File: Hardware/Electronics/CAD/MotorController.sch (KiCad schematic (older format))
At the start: 11 parts, among them J1 MPE 094-1-006, J2 CONN_01X03, J5 CONN_01X04, SW2 SW_DPST_x2, U1 LD1117S33CTR, U2 Nema17, U3 TMC2130, U4 ESP-12E

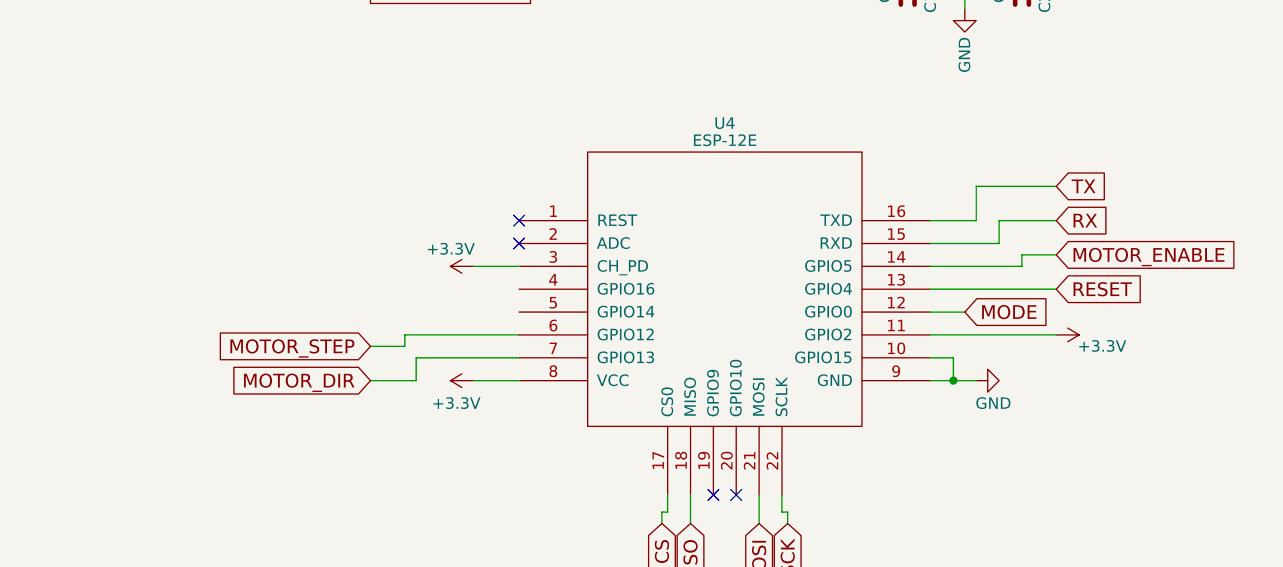
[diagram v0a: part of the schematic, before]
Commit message: home automation iplementation of motor controller software
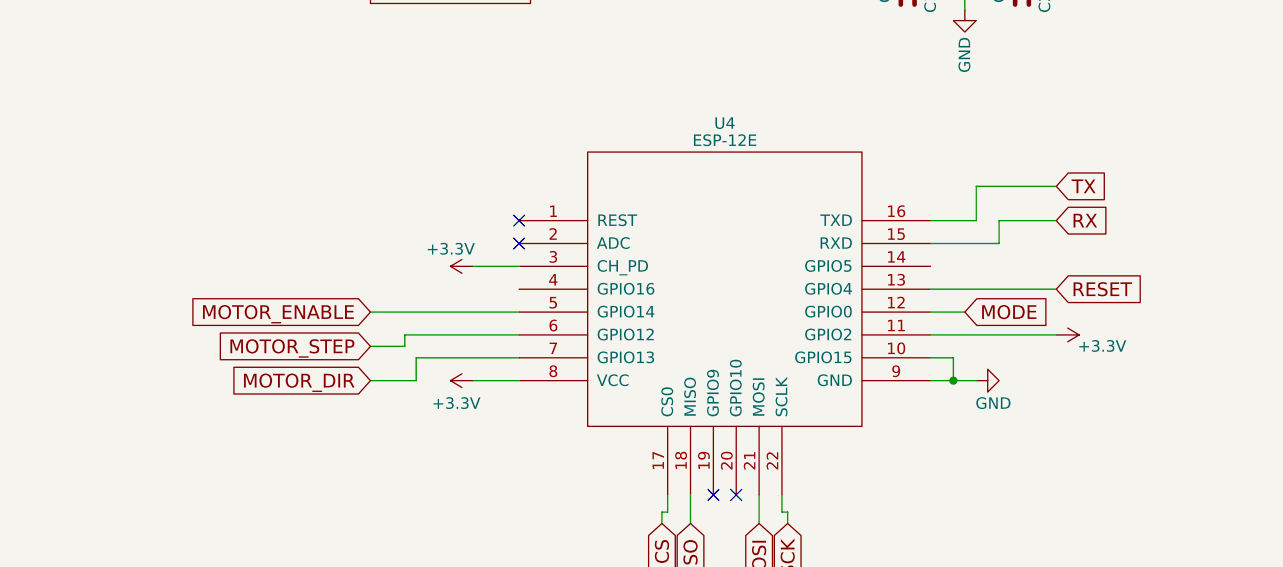
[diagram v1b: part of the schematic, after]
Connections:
- net MOTOR_ENABLE: now also U4.5 (GPIO14); no longer U4.14 (GPIO5)
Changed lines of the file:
@@
 LIBS:Nema17
 LIBS:TMC2130
-LIBS:iot_motor_controller_controller-cache
+LIBS:MotorController-cache
 EELAYER 25 0
 EELAYER END
@@
 NoConn ~ 7000 1400
 NoConn ~ 7000 1500
-Text GLabel 9100 2900 2    60   Input ~ 0
+Text GLabel 6100 3150 0    60   Input ~ 0
 MOTOR_ENABLE
 Wire Wire Line
@@
 Wire Wire Line
 	7000 1700 7100 1700
-Wire Wire Line
-	8550 2950 8950 2950
-Wire Wire Line
-	8950 2950 8950 2900
-Wire Wire Line
-	8950 2900 9100 2900
 Wire Wire Line
 	8550 2850 8850 2850
@@
 NoConn ~ 8250 5075
 NoConn ~ 6750 2850
+Wire Wire Line
+	6750 3150 6100 3150
 $EndSCHEMATC

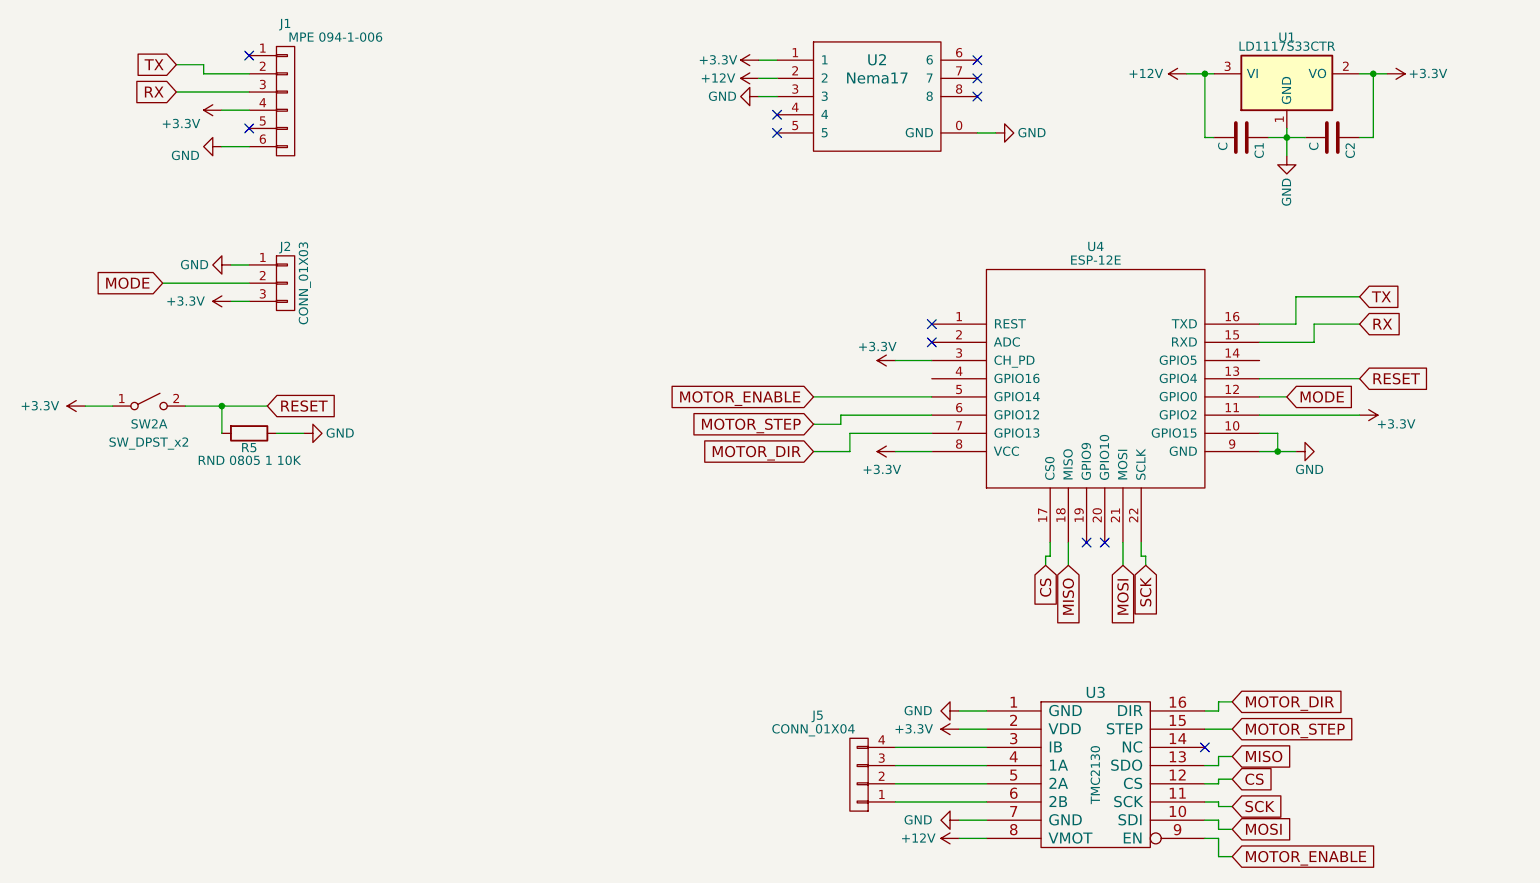
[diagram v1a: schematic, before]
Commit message: new software file structure
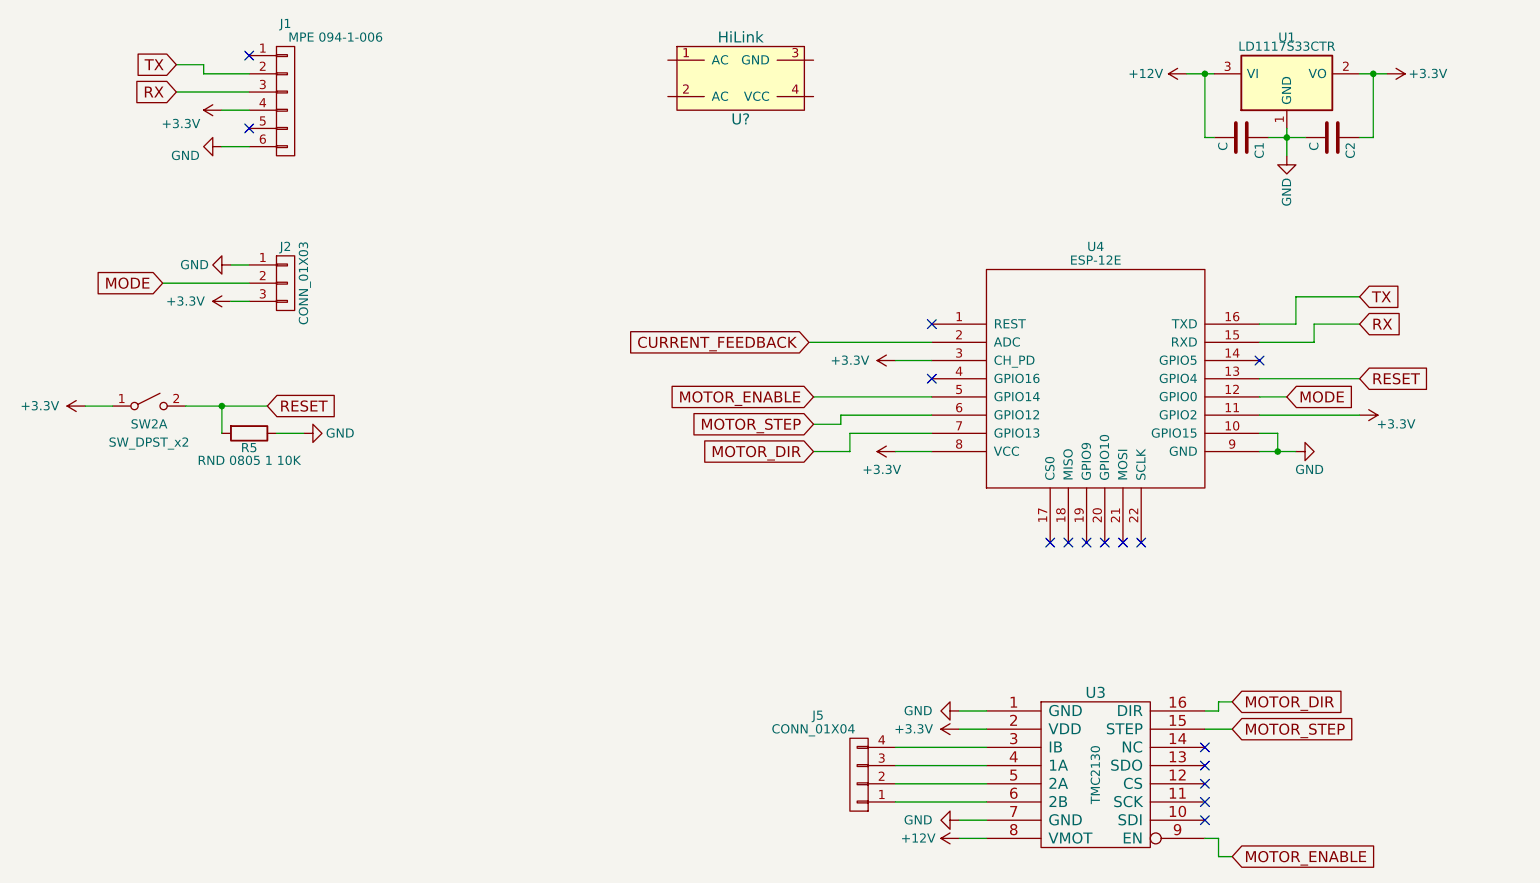
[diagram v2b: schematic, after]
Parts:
- removed U2: Nema17, Nema17:Nema17, symbol Nema17
- added U?: HiLink, symbol HiLink
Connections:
- net CURRENT_FEEDBACK: now reaches U4.2 (ADC)
- net CS: no longer names the net of U4.17 (CS0)
- net CS: no longer U3.12 (CS)
- net MISO: no longer names the net of U4.18 (MISO)
- net MISO: no longer U3.13 (SDO)
- net MOSI: no longer names the net of U4.21 (MOSI)
- net MOSI: no longer U3.10 (SDI)
- net SCK: no longer names the net of U4.22 (SCLK)
- net SCK: no longer U3.11 (SCK)
- no-connect marks 12 -> 16
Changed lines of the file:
@@
 LIBS:Nema17
 LIBS:TMC2130
+LIBS:MAX471
 LIBS:MotorController-cache
 EELAYER 25 0
@@
 P 6550 2950
 F 0 "#PWR03" H 6550 2800 50  0001 C CNN
-F 1 "+3.3V" V 6625 3050 50  0000 C CNN
+F 1 "+3.3V" V 6550 3200 50  0000 C CNN
 F 2 "" H 6550 2950 50  0001 C CNN
 F 3 "" H 6550 2950 50  0001 C CNN
@@
 	0    -1   -1   0
 $EndComp
-$Comp
-L Nema17 U2
-U 1 1 5A280431
-P 6450 1500
-F 0 "U2" H 6450 1700 60  0000 C CNN
-F 1 "Nema17" H 6450 1600 60  0000 C CNN
-F 2 "Nema17:Nema17" H 6450 1500 60  0001 C CNN
-F 3 "" H 6450 1500 60  0001 C CNN
-	1    6450 1500
-	1    0    0    -1
-$EndComp
-$Comp
-L +3.3V #PWR011
-U 1 1 5A281267
-P 5800 1300
-F 0 "#PWR011" H 5800 1150 50  0001 C CNN
-F 1 "+3.3V" V 5800 1525 50  0000 C CNN
-F 2 "" H 5800 1300 50  0001 C CNN
-F 3 "" H 5800 1300 50  0001 C CNN
-	1    5800 1300
-	0    -1   -1   0
-$EndComp
-$Comp
-L GND #PWR012
-U 1 1 5A281299
-P 5800 1500
-F 0 "#PWR012" H 5800 1250 50  0001 C CNN
-F 1 "GND" V 5800 1300 50  0000 C CNN
-F 2 "" H 5800 1500 50  0001 C CNN
-F 3 "" H 5800 1500 50  0001 C CNN
-	1    5800 1500
-	0    1    1    0
-$EndComp
-$Comp
-L +12V #PWR013
-U 1 1 5A28149F
-P 5800 1400
-F 0 "#PWR013" H 5800 1250 50  0001 C CNN
-F 1 "+12V" V 5800 1625 50  0000 C CNN
-F 2 "" H 5800 1400 50  0001 C CNN
-F 3 "" H 5800 1400 50  0001 C CNN
-	1    5800 1400
-	0    -1   -1   0
-$EndComp
-$Comp
-L GND #PWR014
-U 1 1 5A281CD9
-P 7100 1700
-F 0 "#PWR014" H 7100 1450 50  0001 C CNN
-F 1 "GND" V 7100 1500 50  0000 C CNN
-F 2 "" H 7100 1700 50  0001 C CNN
-F 3 "" H 7100 1700 50  0001 C CNN
-	1    7100 1700
-	0    -1   -1   0
-$EndComp
-NoConn ~ 7000 1400
-NoConn ~ 7000 1500
 Text GLabel 6100 3150 0    60   Input ~ 0
 MOTOR_ENABLE
@@
 Wire Wire Line
 	9100 3050 8550 3050
-Wire Wire Line
-	5800 1300 5900 1300
-Wire Wire Line
-	5800 1400 5900 1400
-Wire Wire Line
-	5900 1500 5800 1500
-Wire Wire Line
-	7000 1700 7100 1700
 Wire Wire Line
 	8550 2850 8850 2850
@@
 Wire Wire Line
 	7050 5575 6900 5575
-NoConn ~ 7000 1300
-NoConn ~ 5900 1600
-NoConn ~ 5900 1700
 $Comp
 L TMC2130 U3
@@
 	1    0    0    -1
 $EndComp
-Text GLabel 8400 5525 2    60   Input ~ 0
-MOSI
-Text GLabel 8400 5125 2    60   Input ~ 0
-MISO
-Text GLabel 8400 5250 2    60   Input ~ 0
-CS
-Text GLabel 8400 5400 2    60   Input ~ 0
-SCK
-Wire Wire Line
-	8250 5175 8325 5175
-Wire Wire Line
-	8325 5175 8325 5125
-Wire Wire Line
-	8325 5125 8400 5125
-Wire Wire Line
-	8400 5250 8325 5250
-Wire Wire Line
-	8325 5250 8325 5275
-Wire Wire Line
-	8325 5275 8250 5275
-Wire Wire Line
-	8250 5375 8325 5375
-Wire Wire Line
-	8325 5375 8325 5400
-Wire Wire Line
-	8325 5400 8400 5400
-Wire Wire Line
-	8250 5475 8325 5475
-Wire Wire Line
-	8325 5475 8325 5525
-Wire Wire Line
-	8325 5525 8400 5525
 Wire Wire Line
 	8250 5575 8325 5575
@@
 Wire Wire Line
 	8325 5675 8400 5675
-Text GLabel 7500 4075 3    60   Input ~ 0
-MISO
-Text GLabel 7375 4075 3    60   Input ~ 0
-CS
-Text GLabel 7925 4075 3    60   Input ~ 0
-SCK
-Text GLabel 7800 4075 3    60   Input ~ 0
-MOSI
-Wire Wire Line
-	7500 4075 7500 3950
-Wire Wire Line
-	7400 3950 7400 4025
-Wire Wire Line
-	7400 4025 7375 4025
-Wire Wire Line
-	7375 4025 7375 4075
-Wire Wire Line
-	7800 3950 7800 4075
-Wire Wire Line
-	7925 4075 7925 4025
-Wire Wire Line
-	7925 4025 7900 4025
-Wire Wire Line
-	7900 4025 7900 3950
 $Comp
 L CONN_01X03 J2
@@
 	3000 2625 2900 2625
 NoConn ~ 8250 5075
-NoConn ~ 6750 2850
 Wire Wire Line
 	6750 3150 6100 3150
+NoConn ~ 8250 5175
+NoConn ~ 8250 5275
+NoConn ~ 8250 5375
+NoConn ~ 8250 5475
+NoConn ~ 8550 2950
+NoConn ~ 6750 3050
+NoConn ~ 7800 3950
+NoConn ~ 7900 3950
+NoConn ~ 7500 3950
+NoConn ~ 7400 3950
+Text GLabel 6075 2850 0    60   Input ~ 0
+CURRENT_FEEDBACK
+Wire Wire Line
+	6750 2850 6075 2850
+$Comp
+L HiLink U?
+U 1 1 5AA9B92D
+P 5700 1400
+F 0 "U?" H 5700 1175 60  0000 C CNN
+F 1 "HiLink" H 5700 1625 60  0000 C CNN
+F 2 "" H 5700 1400 60  0001 C CNN
+F 3 "" H 5700 1400 60  0001 C CNN
+	1    5700 1400
+	1    0    0    -1
+$EndComp
 $EndSCHEMATC
